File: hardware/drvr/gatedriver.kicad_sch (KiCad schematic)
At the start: 4 parts

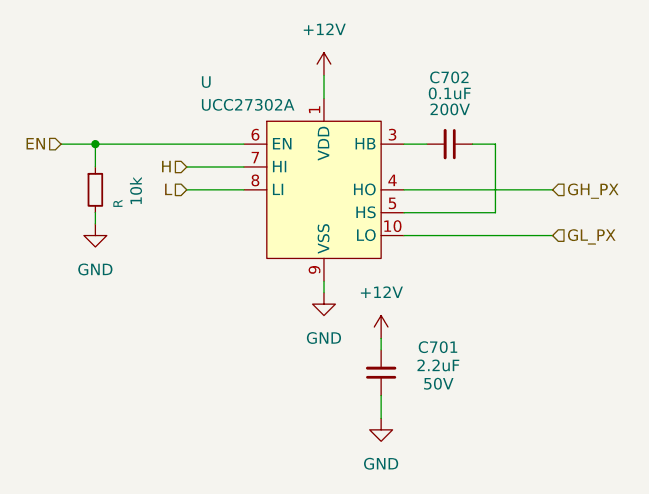
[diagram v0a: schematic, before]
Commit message: added gate driver footprint
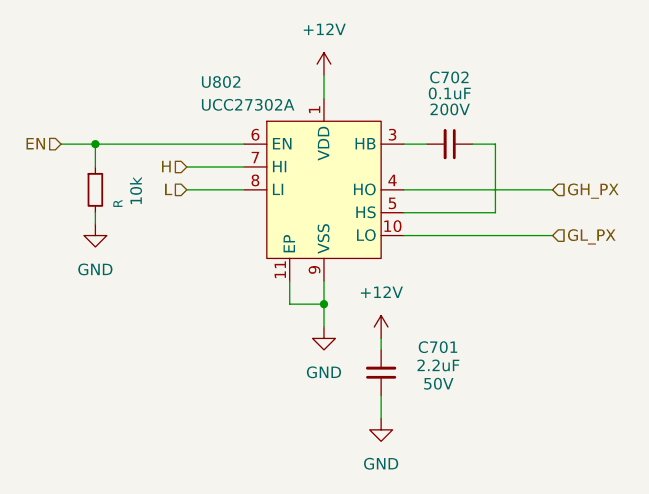
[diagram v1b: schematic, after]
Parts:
- U802: renamed from U; footprint (none) -> mcrmv:DRC0010J-VSON-10
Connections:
- net GND: now also U802.11 (EP)
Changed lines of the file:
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@@
+	)
+	(junction
+		(at 120.65 96.52)
+		(diameter 0)
+		(color 0 0 0 0)
 	)
 	(junction
@@
 	(wire
 		(pts
+			(xy 116.84 96.52) (xy 120.65 96.52)
+		)
+		(stroke
+			(width 0)
+			(type default)
+		)
+	)
+	(wire
+		(pts
 			(xy 105.41 83.82) (xy 111.76 83.82)
 		)
@@
 	(wire
 		(pts
-			(xy 120.65 93.98) (xy 120.65 95.25)
+			(xy 120.65 93.98) (xy 120.65 96.52)
 		)
 		(stroke
@@
 	(wire
 		(pts
+			(xy 116.84 93.98) (xy 116.84 96.52)
+		)
+		(stroke
+			(width 0)
+			(type default)
+		)
+	)
+	(wire
+		(pts
 			(xy 95.25 78.74) (xy 111.76 78.74)
 		)
@@
 		(pts
 			(xy 95.25 86.36) (xy 95.25 87.63)
+		)
+		(stroke
+			(width 0)
+			(type default)
+		)
+	)
+	(wire
+		(pts
+			(xy 120.65 96.52) (xy 120.65 99.06)
 		)
 		(stroke
@@
 		(on_board yes)
 		(dnp no)
-		(property "Reference" "U"
+		(property "Reference" "U802"
 			(at 106.934 71.882 0)
 			(effects
@@
 			)
 		)
-		(property "Footprint" ""
+		(property "Footprint" "mcrmv:DRC0010J-VSON-10"
 			(at 114.3 76.2 0)
 			(effects
@@
 		)
 		(pin "1"
+		)
+		(pin "11"
 		)
 		(instances
 			(project "drvr"
 				(path "/81ae36e8-9cac-4279-b747-86fcffa363b5/87bd7111-59a3-4ada-993e-96677a40981d"
+					(reference "U802")
+					(unit 1)
+				)
+				(path "/81ae36e8-9cac-4279-b747-86fcffa363b5/910a803c-34b5-4d88-a9f3-cf236218f1b3"
 					(reference "U802")
 					(unit 1)
@@
 	(symbol
 		(lib_id "power:GND")
-		(at 120.65 95.25 0)
+		(at 120.65 99.06 0)
+		(mirror y)
 		(unit 1)
 		(exclude_from_sim no)
@@
 		(on_board yes)
 		(dnp no)
-		(fields_autoplaced yes)
 		(property "Reference" "#PWR0704"
-			(at 120.65 101.6 0)
+			(at 120.65 105.41 0)
 			(effects
 				(font
@@
 		)
 		(property "Value" "GND"
-			(at 120.65 100.33 0)
+			(at 120.65 104.14 0)
 			(effects
 				(font
@@
 		)
 		(property "Footprint" ""
-			(at 120.65 95.25 0)
+			(at 120.65 99.06 0)
 			(effects
 				(font
@@
 		)
 		(property "Datasheet" ""
-			(at 120.65 95.25 0)
+			(at 120.65 99.06 0)
 			(effects
 				(font
@@
 		)
 		(property "Description" "Power symbol creates a global label with name \"GND\" , ground"
-			(at 120.65 95.25 0)
-			(effects
-				(font
+			(at 120.65 99.06 0)
+			(effects
+				(font

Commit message: added gatedrivers + pico as draft
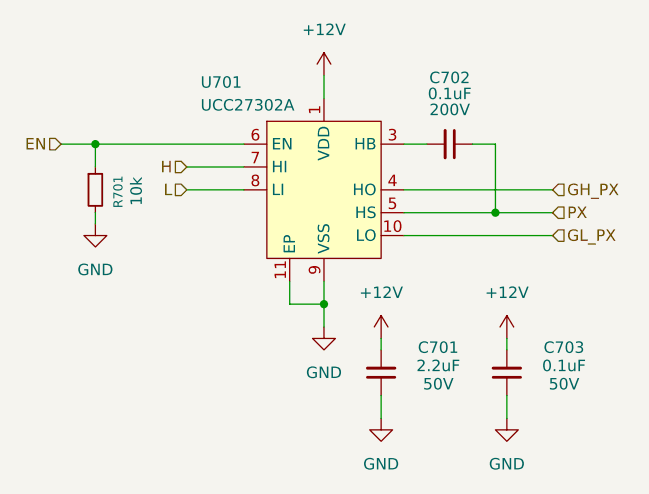
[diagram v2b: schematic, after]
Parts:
- added C703: 0.1uF, Capacitor_SMD:C_0402_1005Metric, symbol Device:C_Small
- renumbered R to R701, U802 to U701
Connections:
- net +12V: now also C703.2
- net GND: now also C703.1
- net PX: now reaches C702.1, U701.5 (HS)
